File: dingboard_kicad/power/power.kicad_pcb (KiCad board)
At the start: 2 copper layers, 0 parts

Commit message: add reference step file from kicad PCIe
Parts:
- added J1: Bus_PCI_Express_x1, Connector_PCBEdge:BUS_PCIexpress_x1, F.Cu at (84.5, 45.0)
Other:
- board outline added: 31 x 10.1 mm
- board text removed: "For Instructional Use Only."
- board text removed: "SOLIDWORKS Educational Product."

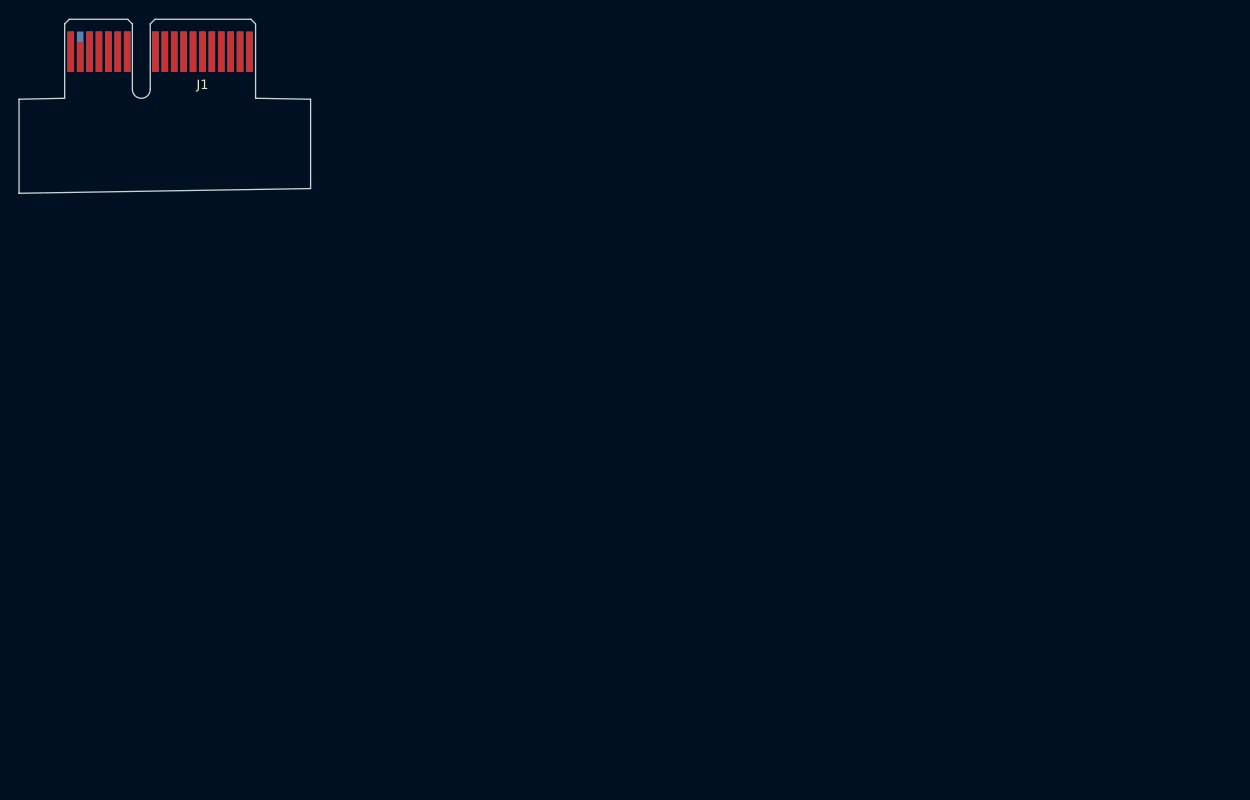
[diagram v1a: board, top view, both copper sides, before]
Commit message: add components to kicad power module
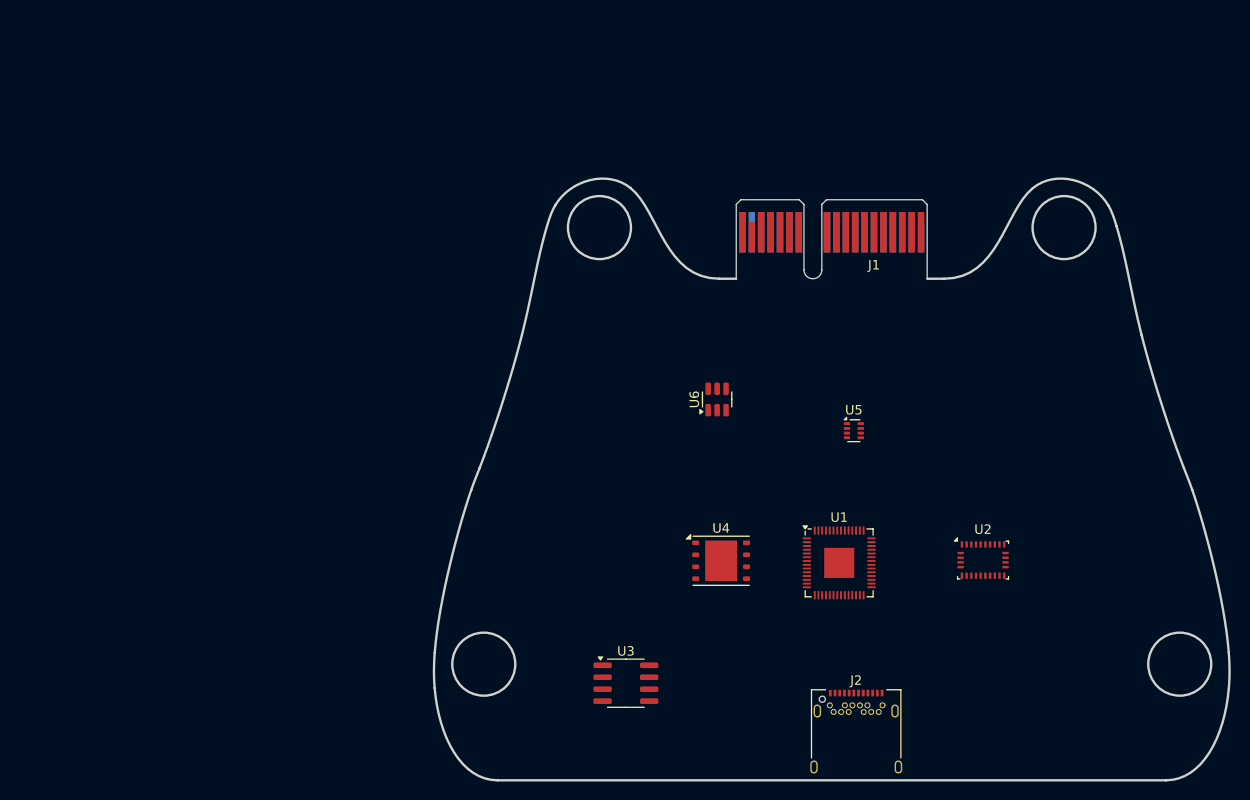
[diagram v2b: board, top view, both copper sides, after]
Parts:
- added J2: USB_C_Receptacle, Connector_USB:USB_C_Receptacle_Amphenol_12401548E4-2A, F.Cu at (149.0, 118.2)
- added U1: RP2040, Package_DFN_QFN:QFN-56-1EP_7x7mm_P0.4mm_EP3.2x3.2mm, F.Cu at (147.2, 99.3)
- added U2: BNO055, Package_LGA:LGA-28_5.2x3.8mm_P0.5mm, F.Cu at (162.5, 99.0)
- added U3: MCP2562-E-SN, Package_SO:SOIC-8_3.9x4.9mm_P1.27mm, F.Cu at (124.5, 112.1)
- added U4: W25Q128JVP, Package_SON:WSON-8-1EP_6x5mm_P1.27mm_EP3.4x4.3mm, F.Cu at (134.7, 99.1)
- added U5: TPS2116DRL, Package_TO_SOT_SMD:SOT-583-8, F.Cu at (148.8, 85.2)
- added U6: LMR51430, Package_TO_SOT_SMD:SOT-23-6, F.Cu at (134.2, 81.9)
- moved J1 73.9 mm to (155.9, 64.1)
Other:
- board size 31 x 10.1 mm -> 84.6 x 64 mm

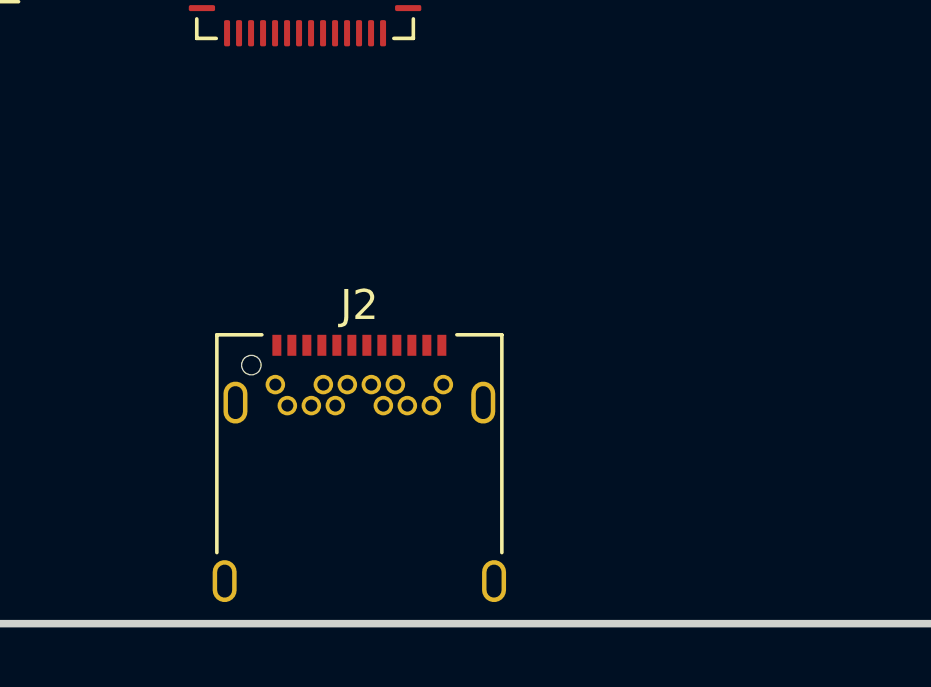
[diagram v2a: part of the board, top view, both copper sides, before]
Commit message: create kicad template
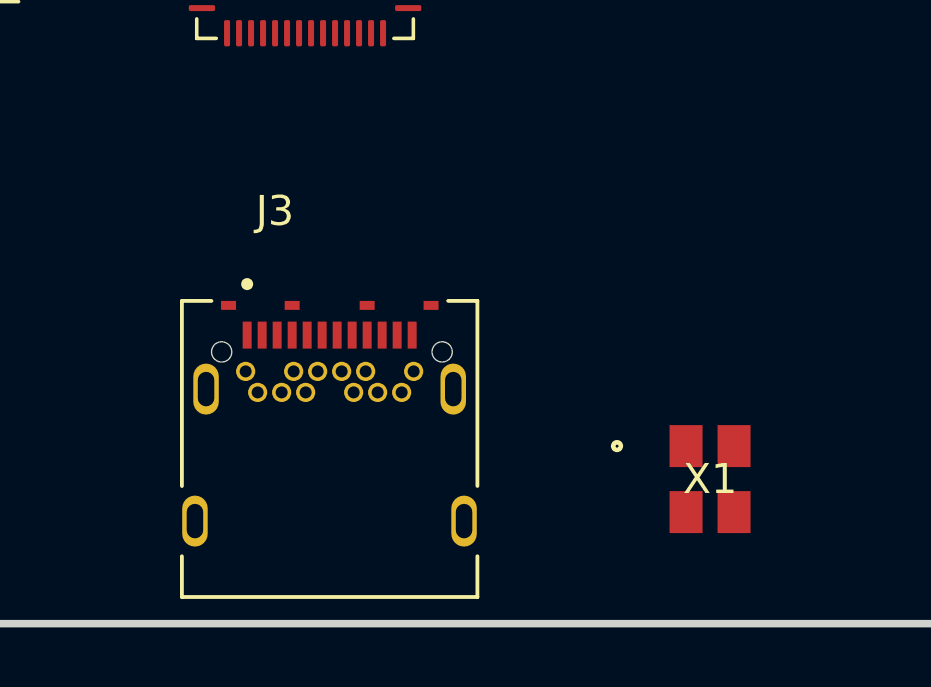
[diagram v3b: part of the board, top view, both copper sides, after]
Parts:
- removed J2: USB_C_Receptacle, Connector_USB:USB_C_Receptacle_Amphenol_12401548E4-2A
- added J3: TYPE-C-31-M-04, TYPE-C-31-M-04:HRO_TYPE-C-31-M-04, F.Cu at (148.0, 112.8)
- added X1: ABM8-272-T3, footprints:ABM8-272-T3_ABR, F.Cu at (160.7, 117.6)
